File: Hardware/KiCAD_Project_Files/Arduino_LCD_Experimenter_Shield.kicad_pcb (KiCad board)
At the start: 2 copper layers, 68.6 x 53.3 mm, 51 parts, among them J1 SFW14R-1STE1LF, P1 1X10 HEADER, P2 1X8 HEADER, P3 1X6 HEADER, P4 1X8 HEADER, P5 2X3 HEADER, SW1 PTS810, SW2 PTS810, SW3 PTS810, SW4 PTS810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

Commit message: Saved files after previous commit, otherwise no change.
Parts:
- moved J1 59.1 mm to (131.4, 104.8), turned to 180 degrees
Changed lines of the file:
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@@
   (general
     (links 143)
-    (no_connects 135)
-    (area 62.134399 42.21734 209.533066 172.7962)
+    (no_connects 134)
+    (area 64.6176 42.21734 209.533066 172.7962)
     (thickness 1.6002)
     (drawings 29)
@@
   )
   (module FFC_14P_1.0MM_SMT (layer Front)
-    (at 72.39 101.6)
-    (fp_text reference J1 (at 0 6.35) (layer F.SilkS)
-      (effects (font (size 1.016 1.016) (thickness 0.2032)))
-    )
-    (fp_text value SFW14R-1STE1LF (at 0 -2.54) (layer F.SilkS)
+    (at 131.445 104.775 180)
+    (fp_text reference J1 (at 0 6.35 180) (layer F.SilkS)
+      (effects (font (size 1.016 1.016) (thickness 0.2032)))
+    )
+    (fp_text value SFW14R-1STE1LF (at 0 -2.54 180) (layer F.SilkS)
       (effects (font (size 1.016 1.016) (thickness 0.2032)))
     )
@@
     (fp_line (start 9.3 0) (end 8.2 0) (layer F.SilkS) (width 0.2032))
     (fp_line (start -9.3 0) (end -8.2 0) (layer F.SilkS) (width 0.2032))
-    (pad 1 smd rect (at 6.5 0) (size 0.6 2) (drill (offset 0 -0.5))
+    (pad 1 smd rect (at 6.5 0 180) (size 0.6 2) (drill (offset 0 -0.5))
       (layers Front F.Paste F.Mask)
       (net 13 D7)
     )
-    (pad 2 smd rect (at 5.5 -0.5) (size 0.6 2)
+    (pad 2 smd rect (at 5.5 -0.5 180) (size 0.6 2)
       (layers Front F.Paste F.Mask)
       (net 12 D6)
     )
-    (pad 3 smd rect (at 4.5 -0.5) (size 0.6 2)
+    (pad 3 smd rect (at 4.5 -0.5 180) (size 0.6 2)
       (layers Front F.Paste F.Mask)
       (net 11 D5)
     )
-    (pad 4 smd rect (at 3.5 -0.5) (size 0.6 2)
+    (pad 4 smd rect (at 3.5 -0.5 180) (size 0.6 2)
       (layers Front F.Paste F.Mask)
       (net 10 D4)
     )
-    (pad 5 smd rect (at 2.5 -0.5) (size 0.6 2)
+    (pad 5 smd rect (at 2.5 -0.5 180) (size 0.6 2)
       (layers Front F.Paste F.Mask)
       (net 9 D3)
     )
-    (pad 6 smd rect (at 1.5 -0.5) (size 0.6 2)
+    (pad 6 smd rect (at 1.5 -0.5 180) (size 0.6 2)
       (layers Front F.Paste F.Mask)
       (net 8 D2)
     )
-    (pad 7 smd rect (at 0.5 -0.5) (size 0.6 2)
+    (pad 7 smd rect (at 0.5 -0.5 180) (size 0.6 2)
       (layers Front F.Paste F.Mask)
       (net 7 D1)
     )
-    (pad 8 smd rect (at -0.5 -0.5) (size 0.6 2)
+    (pad 8 smd rect (at -0.5 -0.5 180) (size 0.6 2)
       (layers Front F.Paste F.Mask)
       (net 6 D0)
     )
-    (pad 9 smd rect (at -1.5 -0.5) (size 0.6 2)
-      (layers Front F.Paste F.Mask)
-      (net 1 +5V)
-    )
-    (pad 10 smd rect (at -2.5 -0.5) (size 0.6 2)
+    (pad 9 smd rect (at -1.5 -0.5 180) (size 0.6 2)
+      (layers Front F.Paste F.Mask)
+      (net 1 +5V)
+    )
+    (pad 10 smd rect (at -2.5 -0.5 180) (size 0.6 2)
       (layers Front F.Paste F.Mask)
       (net 14 E)
     )
-    (pad 11 smd rect (at -3.5 -0.5) (size 0.6 2)
+    (pad 11 smd rect (at -3.5 -0.5 180) (size 0.6 2)
       (layers Front F.Paste F.Mask)
       (net 45 RW)
     )
-    (pad 12 smd rect (at -4.5 -0.5) (size 0.6 2)
+    (pad 12 smd rect (at -4.5 -0.5 180) (size 0.6 2)
       (layers Front F.Paste F.Mask)
       (net 21 IO9)
     )
-    (pad 13 smd rect (at -5.5 -0.5) (size 0.6 2)
+    (pad 13 smd rect (at -5.5 -0.5 180) (size 0.6 2)
       (layers Front F.Paste F.Mask)
       (net 46 V0)
     )
-    (pad 14 smd rect (at -6.5 -0.5) (size 0.6 2)
-      (layers Front F.Paste F.Mask)
-      (net 15 GND)
-    )
-    (pad 15 smd rect (at 7.5 0) (size 0.7 4.2) (drill (offset 0 1.6))
-      (layers Front F.Paste F.Mask)
-    )
-    (pad 16 smd rect (at -7.5 0) (size 0.7 4.2) (drill (offset 0 1.6))
-      (layers Front F.Paste F.Mask)
-    )
+    (pad 14 smd rect (at -6.5 -0.5 180) (size 0.6 2)
+      (layers Front F.Paste F.Mask)
+      (net 15 GND)
+    )
+    (pad 15 smd rect (at 7.5 0 180) (size 0.7 4.2) (drill (offset 0 1.6))
+      (layers Front F.Paste F.Mask)
+    )
+    (pad 16 smd rect (at -7.5 0 180) (size 0.7 4.2) (drill (offset 0 1.6))
+      (layers Front F.Paste F.Mask)
+    )

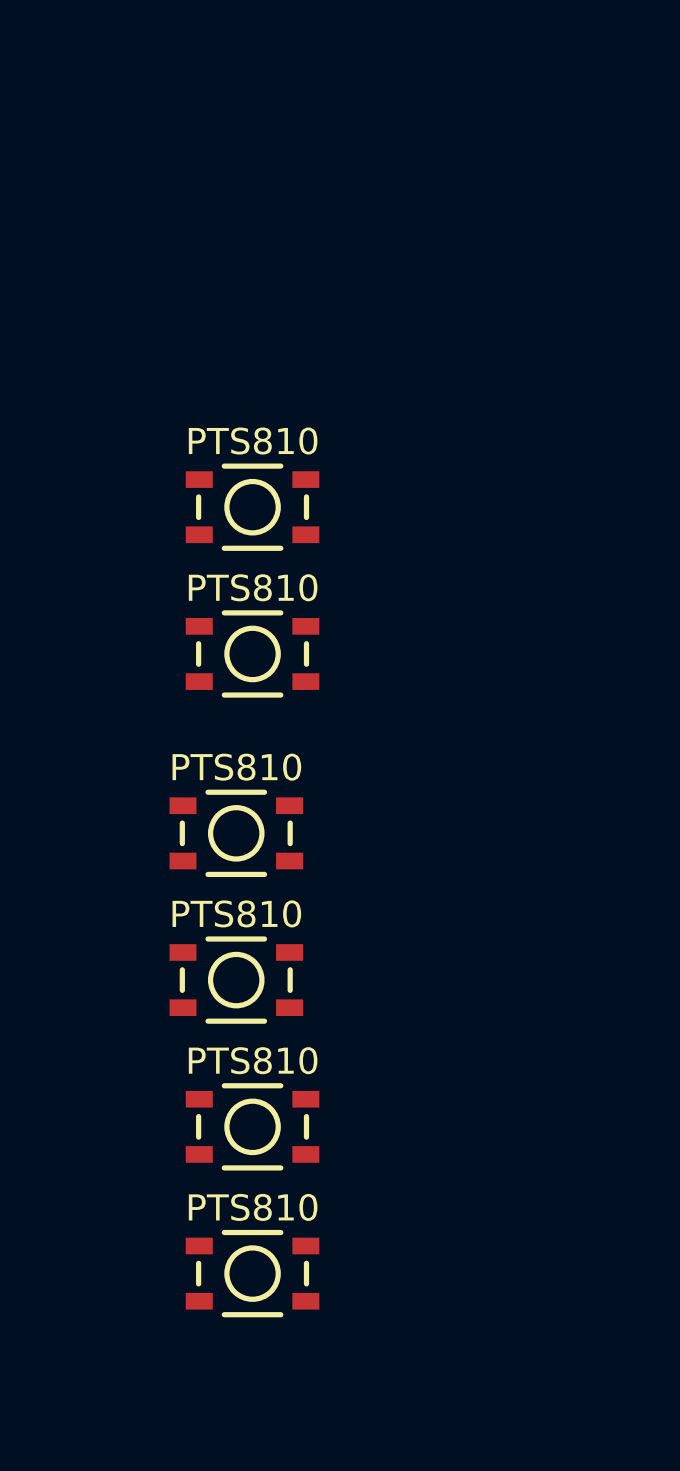
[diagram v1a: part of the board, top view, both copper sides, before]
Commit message: Updated layout to include transducer and pushbutton footprints with 3D models.
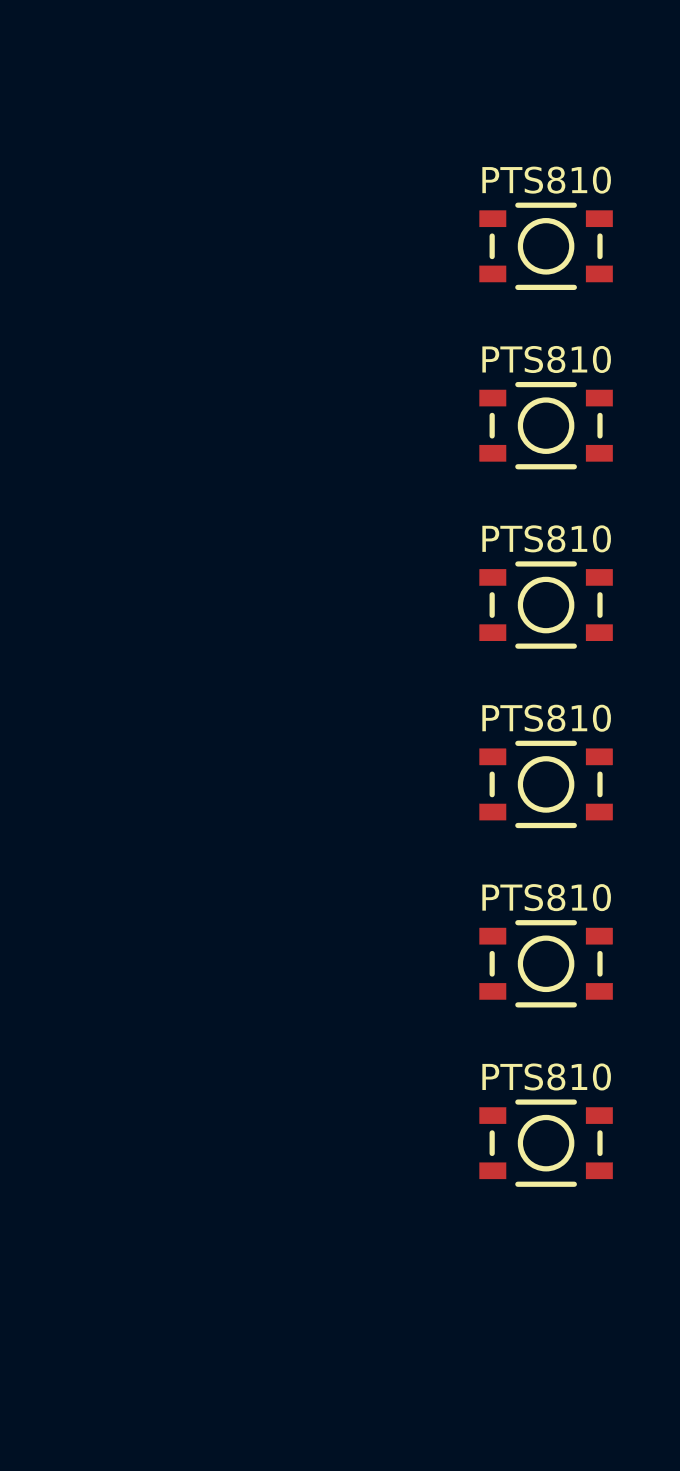
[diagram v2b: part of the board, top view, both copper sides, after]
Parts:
- moved SW4 22.2 mm to (208.3, 96.5)
- moved SW1 19.6 mm to (208.3, 75.6)
- moved SW3 15.0 mm to (208.3, 89.5)
- moved SW5 12.1 mm to (208.3, 103.5)
- moved SW2 11.9 mm to (208.3, 82.5)
- moved SW6 11.4 mm to (208.3, 110.5)
